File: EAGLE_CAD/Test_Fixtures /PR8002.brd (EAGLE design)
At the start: 118.5 x 99.3 mm, 59 parts, among them J1 M3_SCREW_POST

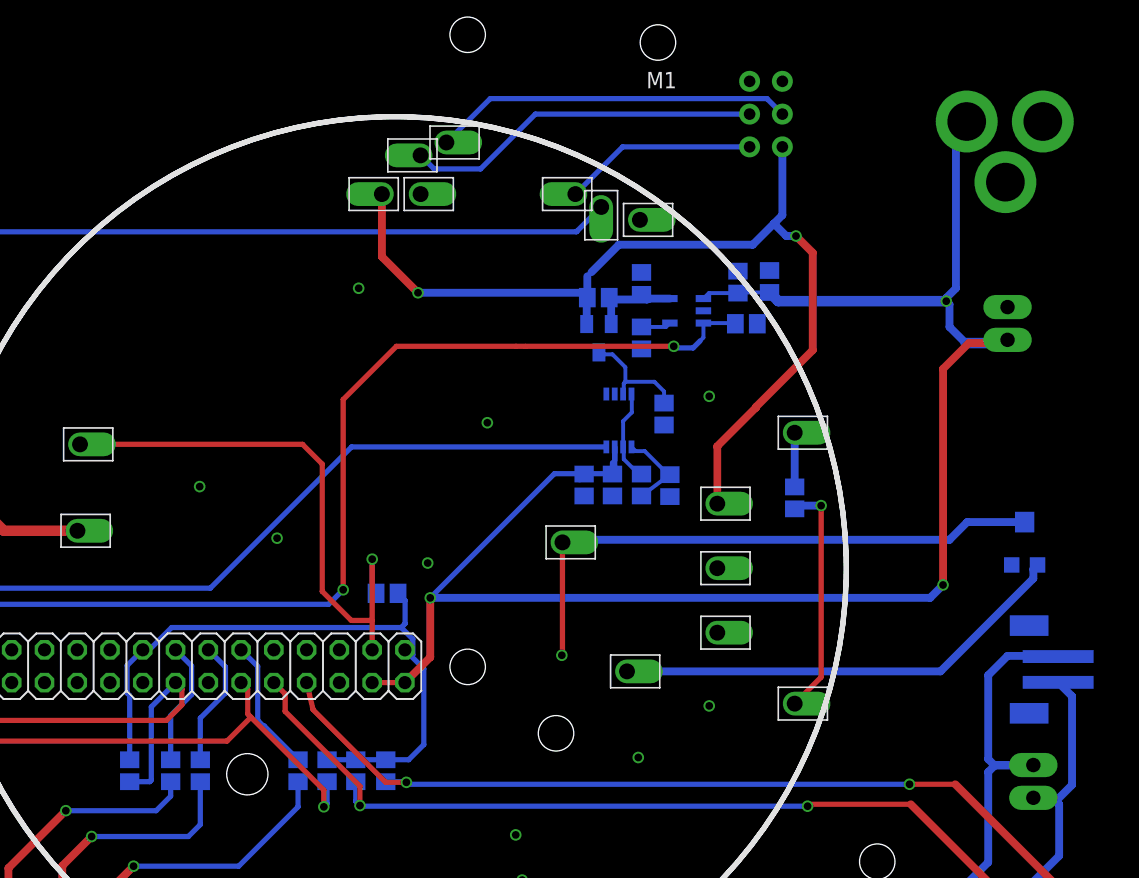
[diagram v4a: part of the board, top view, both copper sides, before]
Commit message: Updated to PR8002
ERC fix
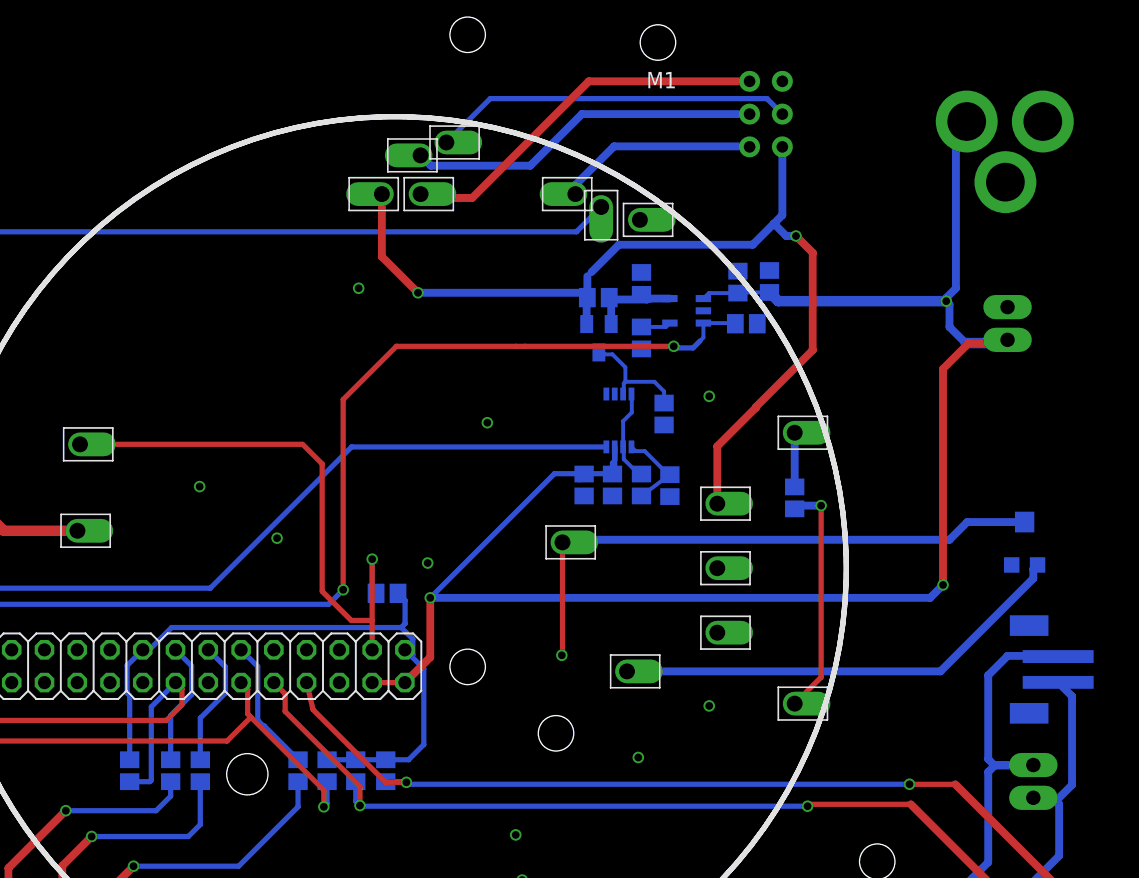
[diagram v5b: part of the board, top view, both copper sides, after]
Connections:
- removed net RESET: U$13.P$1
- net RST: now also U$13.P$1
- net SPK_OUT-: now also JP2.1
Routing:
- net RST: track 0.00 -> 29.4 mm
- net SPK_OUT-: track 76.3 -> 78.3 mm
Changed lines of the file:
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@@
 <wire x1="87.75" y1="53.65" x2="87.5" y2="53.4" width="0.6096" layer="16"/>
-</signal>
-<signal name="RESET">
-<contactref element="U$13" pad="P$1"/>
 </signal>
 <signal name="SW_OUT">
@@
 <wire x1="109" y1="32" x2="109" y2="38.875" width="0.6096" layer="16"/>
 <wire x1="109" y1="38.875" x2="107.925" y2="39.95" width="0.6096" layer="16"/>
-<wire x1="108" y1="30.5" x2="108" y2="31" width="0" layer="19" extent="16-16"/>
-</signal>
-<signal name="MISO">
-<contactref element="U$11" pad="P$1"/>
-<contactref element="ISP1" pad="1"/>
-<wire x1="84.005" y1="81.46" x2="74.16" y2="81.46" width="0.4064" layer="16"/>
-<wire x1="74.16" y1="81.46" x2="70.5" y2="77.8" width="0.4064" layer="16"/>
-</signal>
-<signal name="SCK">
-<contactref element="ISP1" pad="3"/>
-<contactref element="U$12" pad="P$1"/>
-<wire x1="84.005" y1="84" x2="67.4" y2="84" width="0.4064" layer="16"/>
-<wire x1="67.4" y1="84" x2="63.15" y2="79.75" width="0.4064" layer="16"/>
-<wire x1="63.15" y1="79.75" x2="59.55" y2="79.75" width="0.4064" layer="16"/>
-<wire x1="59.55" y1="79.75" x2="58.5" y2="80.8" width="0.4064" layer="16"/>
+<contactref element="JP2" pad="1"/>
+<wire x1="106" y1="31" x2="107.5" y2="31" width="0.4064" layer="16"/>
+<wire x1="107.5" y1="31" x2="108" y2="31" width="0.4064" layer="16"/>
 </signal>
 <signal name="MOSI">
@@
 <signal name="RST">
 <contactref element="ISP1" pad="5"/>
+<contactref element="U$13" pad="P$1"/>
+<wire x1="84.005" y1="86.54" x2="71.54" y2="86.54" width="0.6096" layer="1"/>
+<wire x1="71.54" y1="86.54" x2="62.5" y2="77.5" width="0.6096" layer="1"/>
+<wire x1="62.5" y1="77.5" x2="58.8" y2="77.5" width="0.6096" layer="1"/>
+<wire x1="58.8" y1="77.5" x2="58.5" y2="77.8" width="0.6096" layer="1"/>
 </signal>
 <signal name="ANT">
@@
 </signal>
 <signal name="DEV_PRES">
-<contactref element="U$2" pad="P$1"/>
 <contactref element="GPIO" pad="3"/>
 <contactref element="R2" pad="2"/>
@@
 <wire x1="54.75" y1="49.5" x2="54.75" y2="47.15" width="0.4064" layer="16"/>
 <wire x1="54.75" y1="47.15" x2="55.05" y2="46.85" width="0.4064" layer="16"/>
-<wire x1="32.1" y1="58.4" x2="49.35" y2="58.4" width="0.4064" layer="1"/>
 <wire x1="49.35" y1="58.4" x2="50.875" y2="56.875" width="0.4064" layer="1"/>
 <wire x1="50.875" y1="56.875" x2="50.875" y2="47" width="0.4064" layer="1"/>
 <wire x1="50.875" y1="47" x2="53.125" y2="44.75" width="0.4064" layer="1"/>
 <wire x1="53.125" y1="44.75" x2="54.745" y2="44.75" width="0.4064" layer="1"/>
+<contactref element="U$2" pad="P$1"/>
+<wire x1="49.35" y1="58.4" x2="32.1" y2="58.4" width="0.4064" layer="1"/>
 </signal>
 <signal name="TAC4">
@@
 <contactref element="GPIO" pad="5"/>
 </signal>
+<signal name="MISO">
+<contactref element="ISP1" pad="1"/>
+<contactref element="U$11" pad="P$1"/>
+<wire x1="70.5" y1="77.8" x2="70.5" y2="78.5" width="0.6096" layer="16"/>
+<wire x1="70.5" y1="78.5" x2="73.5" y2="81.5" width="0.6096" layer="16"/>
+<wire x1="73.5" y1="81.5" x2="83.965" y2="81.5" width="0.6096" layer="16"/>
+<wire x1="83.965" y1="81.5" x2="84.005" y2="81.46" width="0.6096" layer="16"/>
+</signal>
+<signal name="SCK">
+<contactref element="ISP1" pad="3"/>
+<contactref element="U$12" pad="P$1"/>
+<wire x1="84.005" y1="84" x2="71" y2="84" width="0.6096" layer="16"/>
+<wire x1="71" y1="84" x2="67" y2="80" width="0.6096" layer="16"/>
+<wire x1="67" y1="80" x2="59.3" y2="80" width="0.6096" layer="16"/>
+<wire x1="59.3" y1="80" x2="58.5" y2="80.8" width="0.6096" layer="16"/>
+</signal>
 </signals>

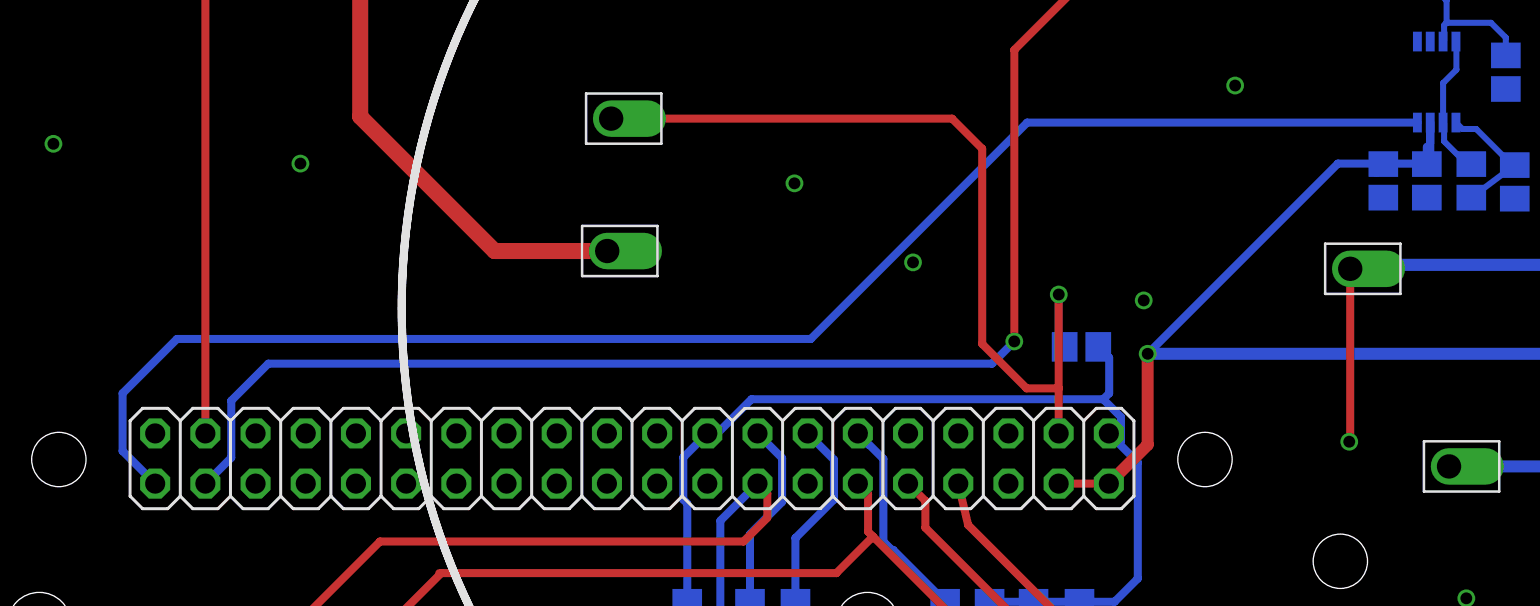
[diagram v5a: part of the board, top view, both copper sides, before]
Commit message: PR8002
Comparator GPIO fix.
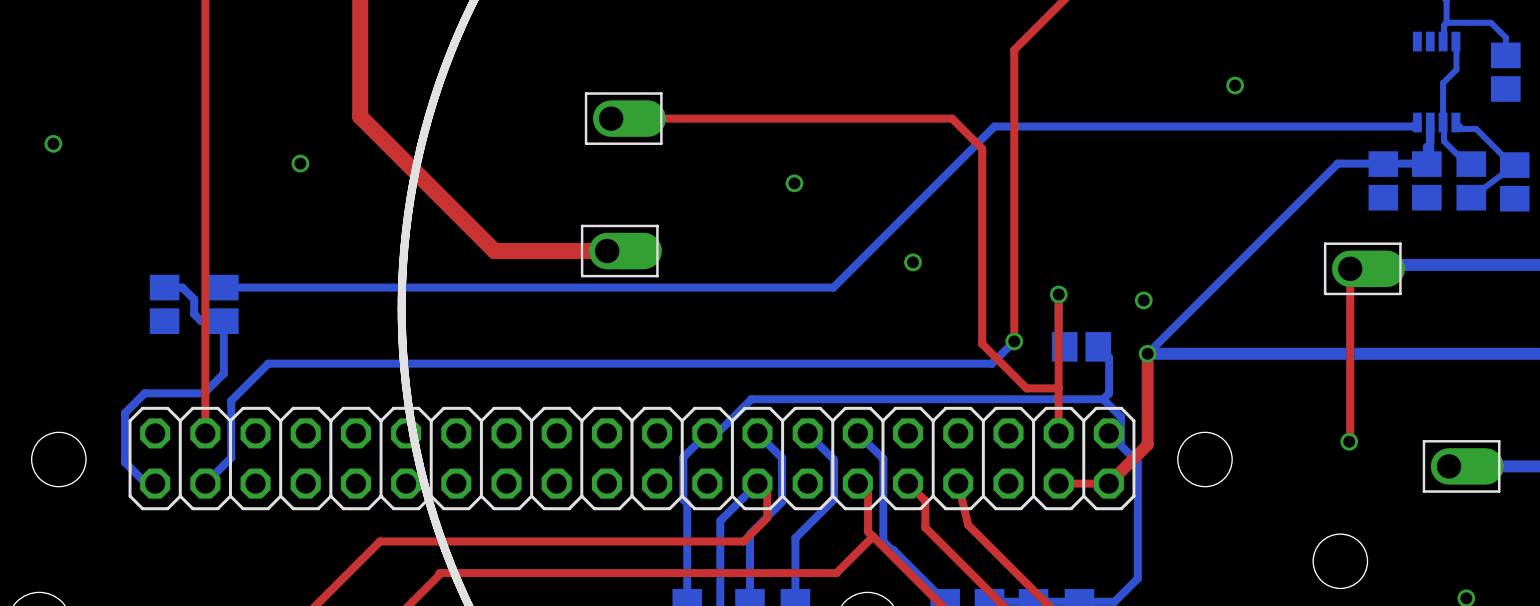
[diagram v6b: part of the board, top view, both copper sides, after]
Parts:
- added R15: 3.3K, PR_Parts_Library:0805_ADAFRUIT
- added R16: 2.2K, PR_Parts_Library:0805_ADAFRUIT
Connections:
- new net N$6: R15.1, TSM931.8
- net COMPARATOR: now also R15.2, R16.1; no longer TSM931.8
- net GND: now also R16.2
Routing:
- net N$6: track 0.00 -> 63.9 mm
- net COMPARATOR: track 76.5 -> 17.1 mm
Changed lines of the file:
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@@
 <setting verticaltext="up"/>
 </settings>
-<grid distance="0.5" unitdist="mm" unit="mm" style="lines" multiple="1" display="yes" altdistance="0.025" altunitdist="inch" altunit="inch"/>
+<grid distance="0.25" unitdist="mm" unit="mm" style="lines" multiple="1" display="yes" altdistance="0.025" altunitdist="inch" altunit="inch"/>
 <layers>
 <layer number="1" name="Top" color="4" fill="1" visible="yes" active="yes"/>
@@
 <element name="JP2" library="SparkFun-Connectors" package="1X02_LONGPADS" value="M02PTH3" x="106" y="31" rot="R90"/>
 <element name="JP3" library="SparkFun-Connectors" package="1X02_LONGPADS" value="M02PTH3" x="104" y="66.5" rot="R90"/>
+<element name="R15" library="PR_Parts_Library" package="0805_ADAFRUIT" value="3.3K" x="12.5" y="49" smashed="yes" rot="MR270">
+<attribute name="TOL" value="" x="12.5" y="49" size="1.27" layer="28" font="vector" ratio="18" rot="MR270" display="off"/>
+<attribute name="MFG_PN" value="" x="12.5" y="49" size="1.27" layer="28" font="vector" ratio="18" rot="MR270" display="off"/>
+<attribute name="POWER" value="" x="12.5" y="49" size="1.27" layer="28" font="vector" ratio="18" rot="MR270" display="off"/>
+<attribute name="NAME" x="12.984" y="54.389" size="1.27" layer="26" font="vector" ratio="16" rot="MR270"/>
+<attribute name="VALUE" x="14.786" y="49.889" size="1.27" layer="28" rot="MR270"/>
+</element>
+<element name="R16" library="PR_Parts_Library" package="0805_ADAFRUIT" value="2.2K" x="9.5" y="49" smashed="yes" rot="MR270">
+<attribute name="TOL" value="" x="9.5" y="49" size="1.27" layer="28" font="vector" ratio="18" rot="MR270" display="off"/>
+<attribute name="MFG_PN" value="" x="9.5" y="49" size="1.27" layer="28" font="vector" ratio="18" rot="MR270" display="off"/>
+<attribute name="POWER" value="" x="9.5" y="49" size="1.27" layer="28" font="vector" ratio="18" rot="MR270" display="off"/>
+<attribute name="NAME" x="9.984" y="54.389" size="1.27" layer="26" font="vector" ratio="16" rot="MR270"/>
+<attribute name="VALUE" x="11.786" y="49.889" size="1.27" layer="28" rot="MR270"/>
+</element>
 </elements>
 <signals>
@@
 <via x="45.875" y="17.625" extent="1-16" drill="0.6"/>
 <contactref element="JP3" pad="2"/>
+<contactref element="R16" pad="2"/>
 </signal>
 <signal name="A_OUT">
@@
 </signal>
 <signal name="COMPARATOR">
-<contactref element="TSM931" pad="8"/>
 <contactref element="GPIO" pad="40"/>
-<wire x1="72.9" y1="58.2" x2="53.15" y2="58.2" width="0.4064" layer="16"/>
-<wire x1="53.15" y1="58.2" x2="42.2" y2="47.25" width="0.4064" layer="16"/>
-<wire x1="42.2" y1="47.25" x2="10.125" y2="47.25" width="0.4064" layer="16"/>
-<wire x1="10.125" y1="47.25" x2="7.375" y2="44.5" width="0.4064" layer="16"/>
-<wire x1="7.375" y1="44.5" x2="7.375" y2="41.58" width="0.4064" layer="16"/>
-<wire x1="7.375" y1="41.58" x2="9.025" y2="39.93" width="0.4064" layer="16"/>
+<contactref element="R15" pad="2"/>
+<contactref element="R16" pad="1"/>
+<wire x1="12.5" y1="48.15" x2="11.35" y2="48.15" width="0.4064" layer="16"/>
+<wire x1="9.025" y1="39.93" x2="8.57" y2="39.93" width="0.4064" layer="16"/>
+<wire x1="8.57" y1="39.93" x2="7.5" y2="41" width="0.4064" layer="16"/>
+<wire x1="7.5" y1="41" x2="7.5" y2="43.5" width="0.4064" layer="16"/>
+<wire x1="7.5" y1="43.5" x2="8.5" y2="44.5" width="0.4064" layer="16"/>
+<wire x1="8.5" y1="44.5" x2="11.5" y2="44.5" width="0.4064" layer="16"/>
+<wire x1="11.5" y1="44.5" x2="12.5" y2="45.5" width="0.4064" layer="16"/>
+<wire x1="12.5" y1="45.5" x2="12.5" y2="48.15" width="0.4064" layer="16"/>
+<wire x1="9.5" y1="49.85" x2="10.4" y2="49.85" width="0.4064" layer="16"/>
+<wire x1="10.4" y1="49.85" x2="11" y2="49.25" width="0.4064" layer="16"/>
+<wire x1="11" y1="49.25" x2="11" y2="48.5" width="0.4064" layer="16"/>
+<wire x1="11" y1="48.5" x2="11.35" y2="48.15" width="0.4064" layer="16"/>
 </signal>
 <signal name="+3V3">
@@
 <wire x1="59.3" y1="80" x2="58.5" y2="80.8" width="0.6096" layer="16"/>
 </signal>
+<signal name="N$6">
+<contactref element="TSM931" pad="8"/>
+<contactref element="R15" pad="1"/>
+<wire x1="12.5" y1="49.85" x2="43.35" y2="49.85" width="0.4064" layer="16"/>
+<wire x1="43.35" y1="49.85" x2="51.5" y2="58" width="0.4064" layer="16"/>
+<wire x1="51.5" y1="58" x2="72.7" y2="58" width="0.4064" layer="16"/>
+<wire x1="72.7" y1="58" x2="72.9" y2="58.2" width="0.4064" layer="16"/>
+</signal>
 </signals>

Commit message: Updates PR8002
Updates PR8002
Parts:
- R15: value 3.3K -> 2.2K
- R16: value 2.2K -> 3.3K
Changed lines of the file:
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@@
 <hole x="93.9" y="26.05" drill="2.75"/>
 <text x="107.5" y="70.5" size="1.27" layer="22" font="vector" ratio="18" rot="MR270">+   -</text>
+<dimension x1="0.5" y1="-0.7" x2="37.75" y2="99.25" x3="126" y3="49.275" textsize="1.27" textratio="18" layer="20" dtype="vertical" unit="inch"/>
+<dimension x1="0.5" y1="99.675" x2="119" y2="99.3" x3="59.75" y3="102.5" textsize="1.27" textratio="18" layer="20" dtype="horizontal" unit="inch"/>
 </plain>
 <attributes>
@@
 <element name="JP2" library="SparkFun-Connectors" package="1X02_LONGPADS" value="M02PTH3" x="106" y="31" rot="R90"/>
 <element name="JP3" library="SparkFun-Connectors" package="1X02_LONGPADS" value="M02PTH3" x="104" y="66.5" rot="R90"/>
-<element name="R15" library="PR_Parts_Library" package="0805_ADAFRUIT" value="3.3K" x="12.5" y="49" smashed="yes" rot="MR270">
+<element name="R15" library="PR_Parts_Library" package="0805_ADAFRUIT" value="2.2K" x="12.5" y="49" smashed="yes" rot="MR270">
 <attribute name="TOL" value="" x="12.5" y="49" size="1.27" layer="28" font="vector" ratio="18" rot="MR270" display="off"/>
 <attribute name="MFG_PN" value="" x="12.5" y="49" size="1.27" layer="28" font="vector" ratio="18" rot="MR270" display="off"/>
@@
 <attribute name="VALUE" x="14.786" y="49.889" size="1.27" layer="28" rot="MR270"/>
 </element>
-<element name="R16" library="PR_Parts_Library" package="0805_ADAFRUIT" value="2.2K" x="9.5" y="49" smashed="yes" rot="MR270">
+<element name="R16" library="PR_Parts_Library" package="0805_ADAFRUIT" value="3.3K" x="9.5" y="49" smashed="yes" rot="MR270">
 <attribute name="TOL" value="" x="9.5" y="49" size="1.27" layer="28" font="vector" ratio="18" rot="MR270" display="off"/>
 <attribute name="MFG_PN" value="" x="9.5" y="49" size="1.27" layer="28" font="vector" ratio="18" rot="MR270" display="off"/>
@@
 <contactref element="ISP1" pad="6"/>
 <polygon width="0.6096" layer="1">
-<vertex x="0.5" y="100.925"/>
-<vertex x="119.875" y="100.425"/>
+<vertex x="0.5" y="99.675"/>
+<vertex x="119.875" y="99.175"/>
 <vertex x="118.875" y="-0.2"/>
 <vertex x="0.5" y="-0.7"/>
@@
 <vertex x="0.5" y="-0.7"/>
 <vertex x="119" y="-0.325"/>
-<vertex x="120" y="101.175"/>
-<vertex x="0" y="101.3"/>
+<vertex x="120" y="99.675"/>
+<vertex x="0" y="99.8"/>
 </polygon>
 <contactref element="U$3" pad="P$1"/>
